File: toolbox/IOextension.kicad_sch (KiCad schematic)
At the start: 19 parts

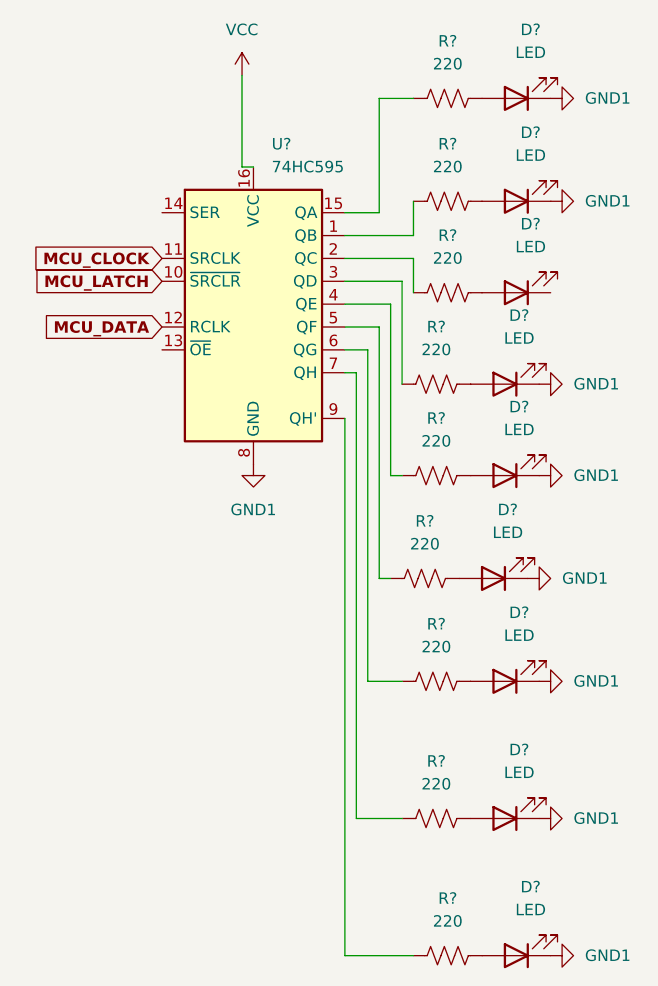
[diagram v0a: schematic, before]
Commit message: added p-mosfet prcotection circuit
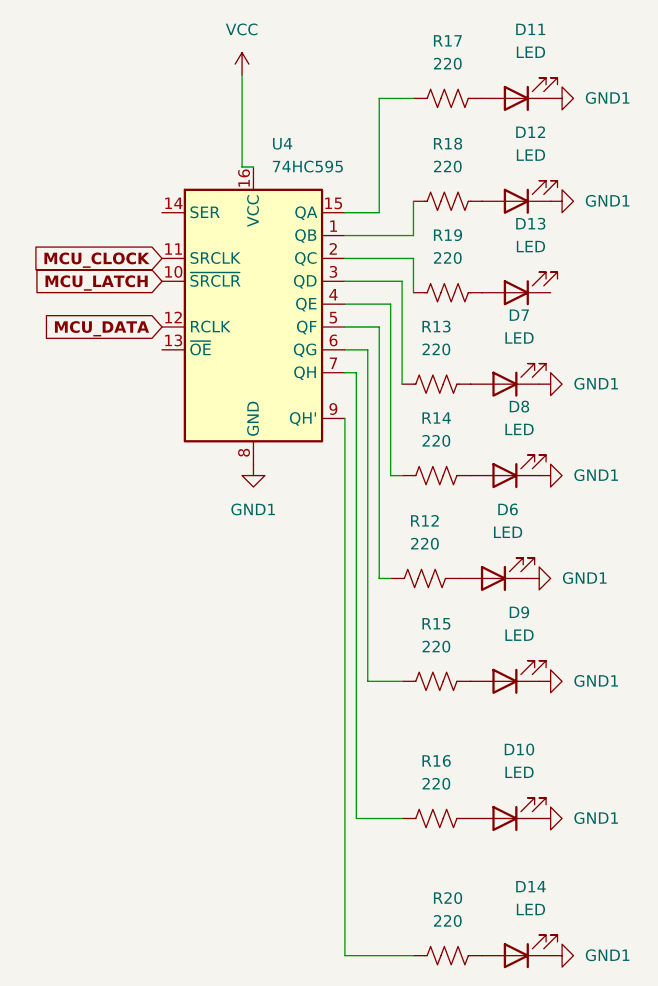
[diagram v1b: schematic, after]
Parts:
- gave numbers to parts that had none: 19
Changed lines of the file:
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@@
   (symbol (lib_id "Device:LED") (at 134.62 109.22 180) (unit 1)
     (in_bom yes) (on_board yes) (fields_autoplaced)
-    (property "Reference" "D?" (id 0) (at 136.2075 101.6 0))
+    (property "Reference" "D6" (id 0) (at 136.2075 101.6 0))
     (property "Value" "LED" (id 1) (at 136.2075 104.14 0))
     (property "Footprint" "" (id 2) (at 134.62 109.22 0)
@@
   (symbol (lib_id "Device:LED") (at 135.89 97.79 180) (unit 1)
     (in_bom yes) (on_board yes) (fields_autoplaced)
-    (property "Reference" "D?" (id 0) (at 137.4775 90.17 0))
+    (property "Reference" "D8" (id 0) (at 137.4775 90.17 0))
     (property "Value" "LED" (id 1) (at 137.4775 92.71 0))
     (property "Footprint" "" (id 2) (at 135.89 97.79 0)
@@
   (symbol (lib_id "Device:R_US") (at 128.27 120.65 90) (unit 1)
     (in_bom yes) (on_board yes) (fields_autoplaced)
-    (property "Reference" "R?" (id 0) (at 128.27 114.3 90))
+    (property "Reference" "R15" (id 0) (at 128.27 114.3 90))
     (property "Value" "220" (id 1) (at 128.27 116.84 90))
     (property "Footprint" "" (id 2) (at 128.524 119.634 90)
@@
   (symbol (lib_id "74xx:74HC595") (at 107.95 78.74 0) (unit 1)
     (in_bom yes) (on_board yes) (fields_autoplaced)
-    (property "Reference" "U?" (id 0) (at 109.9694 60.96 0)
+    (property "Reference" "U4" (id 0) (at 109.9694 60.96 0)
       (effects (font (size 1.27 1.27)) (justify left))
     )
@@
   (symbol (lib_id "power:GND1") (at 139.7 120.65 90) (unit 1)
     (in_bom yes) (on_board yes) (fields_autoplaced)
-    (property "Reference" "#PWR?" (id 0) (at 146.05 120.65 0)
+    (property "Reference" "#PWR027" (id 0) (at 146.05 120.65 0)
       (effects (font (size 1.27 1.27)) hide)
     )
@@
   (symbol (lib_id "Device:LED") (at 135.89 120.65 180) (unit 1)
     (in_bom yes) (on_board yes) (fields_autoplaced)
-    (property "Reference" "D?" (id 0) (at 137.4775 113.03 0))
+    (property "Reference" "D9" (id 0) (at 137.4775 113.03 0))
     (property "Value" "LED" (id 1) (at 137.4775 115.57 0))
     (property "Footprint" "" (id 2) (at 135.89 120.65 0)
@@
   (symbol (lib_id "Device:R_US") (at 129.54 151.13 90) (unit 1)
     (in_bom yes) (on_board yes) (fields_autoplaced)
-    (property "Reference" "R?" (id 0) (at 129.54 144.78 90))
+    (property "Reference" "R20" (id 0) (at 129.54 144.78 90))
     (property "Value" "220" (id 1) (at 129.54 147.32 90))
     (property "Footprint" "" (id 2) (at 129.794 150.114 90)
@@
   (symbol (lib_id "Device:R_US") (at 127 109.22 90) (unit 1)
     (in_bom yes) (on_board yes) (fields_autoplaced)
-    (property "Reference" "R?" (id 0) (at 127 102.87 90))
+    (property "Reference" "R12" (id 0) (at 127 102.87 90))
     (property "Value" "220" (id 1) (at 127 105.41 90))
     (property "Footprint" "" (id 2) (at 127.254 108.204 90)
@@
   (symbol (lib_id "power:GND1") (at 139.7 135.89 90) (unit 1)
     (in_bom yes) (on_board yes) (fields_autoplaced)
-    (property "Reference" "#PWR?" (id 0) (at 146.05 135.89 0)
+    (property "Reference" "#PWR028" (id 0) (at 146.05 135.89 0)
       (effects (font (size 1.27 1.27)) hide)
     )
@@
   (symbol (lib_id "Device:R_US") (at 129.54 55.88 90) (unit 1)
     (in_bom yes) (on_board yes) (fields_autoplaced)
-    (property "Reference" "R?" (id 0) (at 129.54 49.53 90))
+    (property "Reference" "R17" (id 0) (at 129.54 49.53 90))
     (property "Value" "220" (id 1) (at 129.54 52.07 90))
     (property "Footprint" "" (id 2) (at 129.794 54.864 90)
@@
   (symbol (lib_id "Device:R_US") (at 128.27 135.89 90) (unit 1)
     (in_bom yes) (on_board yes) (fields_autoplaced)
-    (property "Reference" "R?" (id 0) (at 128.27 129.54 90))
+    (property "Reference" "R16" (id 0) (at 128.27 129.54 90))
     (property "Value" "220" (id 1) (at 128.27 132.08 90))
     (property "Footprint" "" (id 2) (at 128.524 134.874 90)
@@
   (symbol (lib_id "power:GND1") (at 139.7 87.63 90) (unit 1)
     (in_bom yes) (on_board yes) (fields_autoplaced)
-    (property "Reference" "#PWR?" (id 0) (at 146.05 87.63 0)
+    (property "Reference" "#PWR025" (id 0) (at 146.05 87.63 0)
       (effects (font (size 1.27 1.27)) hide)
     )
@@
   (symbol (lib_id "power:GND1") (at 139.7 97.79 90) (unit 1)
     (in_bom yes) (on_board yes) (fields_autoplaced)
-    (property "Reference" "#PWR?" (id 0) (at 146.05 97.79 0)
+    (property "Reference" "#PWR026" (id 0) (at 146.05 97.79 0)
       (effects (font (size 1.27 1.27)) hide)
     )
@@
   (symbol (lib_id "Device:LED") (at 137.16 55.88 180) (unit 1)
     (in_bom yes) (on_board yes) (fields_autoplaced)
-    (property "Reference" "D?" (id 0) (at 138.7475 48.26 0))
+    (property "Reference" "D11" (id 0) (at 138.7475 48.26 0))
     (property "Value" "LED" (id 1) (at 138.7475 50.8 0))
     (property "Footprint" "" (id 2) (at 137.16 55.88 0)
@@
   (symbol (lib_id "Device:R_US") (at 128.27 87.63 90) (unit 1)
     (in_bom yes) (on_board yes) (fields_autoplaced)
-    (property "Reference" "R?" (id 0) (at 128.27 81.28 90))
+    (property "Reference" "R13" (id 0) (at 128.27 81.28 90))
     (property "Value" "220" (id 1) (at 128.27 83.82 90))
     (property "Footprint" "" (id 2) (at 128.524 86.614 90)
@@
   (symbol (lib_id "power:GND1") (at 140.97 55.88 90) (unit 1)
     (in_bom yes) (on_board yes) (fields_autoplaced)
-    (property "Reference" "#PWR?" (id 0) (at 147.32 55.88 0)
+    (property "Reference" "#PWR029" (id 0) (at 147.32 55.88 0)
       (effects (font (size 1.27 1.27)) hide)
     )
@@
   (symbol (lib_id "Device:LED") (at 137.16 67.31 180) (unit 1)
     (in_bom yes) (on_board yes) (fields_autoplaced)
-    (property "Reference" "D?" (id 0) (at 138.7475 59.69 0))
+    (property "Reference" "D12" (id 0) (at 138.7475 59.69 0))
     (property "Value" "LED" (id 1) (at 138.7475 62.23 0))
     (property "Footprint" "" (id 2) (at 137.16 67.31 0)
@@
   (symbol (lib_id "Device:LED") (at 137.16 151.13 180) (unit 1)
     (in_bom yes) (on_board yes) (fields_autoplaced)
-    (property "Reference" "D?" (id 0) (at 138.7475 143.51 0))
+    (property "Reference" "D14" (id 0) (at 138.7475 143.51 0))
     (property "Value" "LED" (id 1) (at 138.7475 146.05 0))
     (property "Footprint" "" (id 2) (at 137.16 151.13 0)
@@
   (symbol (lib_id "power:GND1") (at 107.95 96.52 0) (unit 1)
     (in_bom yes) (on_board yes) (fields_autoplaced)
-    (property "Reference" "#PWR?" (id 0) (at 107.95 102.87 0)
+    (property "Reference" "#PWR023" (id 0) (at 107.95 102.87 0)
       (effects (font (size 1.27 1.27)) hide)
     )
@@
   (symbol (lib_id "Device:LED") (at 137.16 77.47 180) (unit 1)
     (in_bom yes) (on_board yes) (fields_autoplaced)
-    (property "Reference" "D?" (id 0) (at 138.7475 69.85 0))
+    (property "Reference" "D13" (id 0) (at 138.7475 69.85 0))
     (property "Value" "LED" (id 1) (at 138.7475 72.39 0))
     (property "Footprint" "" (id 2) (at 137.16 77.47 0)
@@
   (symbol (lib_id "Device:LED") (at 135.89 87.63 180) (unit 1)
     (in_bom yes) (on_board yes) (fields_autoplaced)
-    (property "Reference" "D?" (id 0) (at 137.4775 80.01 0))
+    (property "Reference" "D7" (id 0) (at 137.4775 80.01 0))
     (property "Value" "LED" (id 1) (at 137.4775 82.55 0))
     (property "Footprint" "" (id 2) (at 135.89 87.63 0)
@@
   (symbol (lib_id "power:GND1") (at 138.43 109.22 90) (unit 1)
     (in_bom yes) (on_board yes) (fields_autoplaced)
-    (property "Reference" "#PWR?" (id 0) (at 144.78 109.22 0)
+    (property "Reference" "#PWR024" (id 0) (at 144.78 109.22 0)
       (effects (font (size 1.27 1.27)) hide)
     )
@@
   (symbol (lib_id "Device:R_US") (at 129.54 77.47 90) (unit 1)
     (in_bom yes) (on_board yes) (fields_autoplaced)
-    (property "Reference" "R?" (id 0) (at 129.54 71.12 90))
+    (property "Reference" "R19" (id 0) (at 129.54 71.12 90))
     (property "Value" "220" (id 1) (at 129.54 73.66 90))
     (property "Footprint" "" (id 2) (at 129.794 76.454 90)
@@
   (symbol (lib_id "Device:LED") (at 135.89 135.89 180) (unit 1)
     (in_bom yes) (on_board yes) (fields_autoplaced)
-    (property "Reference" "D?" (id 0) (at 137.4775 128.27 0))
+    (property "Reference" "D10" (id 0) (at 137.4775 128.27 0))
     (property "Value" "LED" (id 1) (at 137.4775 130.81 0))
     (property "Footprint" "" (id 2) (at 135.89 135.89 0)
@@
   (symbol (lib_id "Device:R_US") (at 128.27 97.79 90) (unit 1)
     (in_bom yes) (on_board yes) (fields_autoplaced)
-    (property "Reference" "R?" (id 0) (at 128.27 91.44 90))
+    (property "Reference" "R14" (id 0) (at 128.27 91.44 90))
     (property "Value" "220" (id 1) (at 128.27 93.98 90))
     (property "Footprint" "" (id 2) (at 128.524 96.774 90)
@@
   (symbol (lib_id "power:GND1") (at 140.97 67.31 90) (unit 1)
     (in_bom yes) (on_board yes) (fields_autoplaced)
-    (property "Reference" "#PWR?" (id 0) (at 147.32 67.31 0)
+    (property "Reference" "#PWR030" (id 0) (at 147.32 67.31 0)
       (effects (font (size 1.27 1.27)) hide)
     )
@@
   (symbol (lib_id "power:VCC") (at 106.68 53.34 0) (unit 1)
     (in_bom yes) (on_board yes) (fields_autoplaced)
-    (property "Reference" "#PWR?" (id 0) (at 106.68 57.15 0)
+    (property "Reference" "#PWR022" (id 0) (at 106.68 57.15 0)
       (effects (font (size 1.27 1.27)) hide)
     )
@@
   (symbol (lib_id "power:GND1") (at 140.97 151.13 90) (unit 1)
     (in_bom yes) (on_board yes) (fields_autoplaced)
-    (property "Reference" "#PWR?" (id 0) (at 147.32 151.13 0)
+    (property "Reference" "#PWR031" (id 0) (at 147.32 151.13 0)
       (effects (font (size 1.27 1.27)) hide)
     )
@@
   (symbol (lib_id "Device:R_US") (at 129.54 67.31 90) (unit 1)
     (in_bom yes) (on_board yes) (fields_autoplaced)
-    (property "Reference" "R?" (id 0) (at 129.54 60.96 90))
+    (property "Reference" "R18" (id 0) (at 129.54 60.96 90))
     (property "Value" "220" (id 1) (at 129.54 63.5 90))
     (property "Footprint" "" (id 2) (at 129.794 66.294 90)
